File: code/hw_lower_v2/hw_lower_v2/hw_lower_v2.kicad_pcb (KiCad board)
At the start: 4 copper layers, 102 x 104.8 mm, 115 parts, among them J1 Screw_Terminal_01x01, J14 Conn_01x02, J2 Screw_Terminal_01x01, J3 Screw_Terminal_01x01, J4 Screw_Terminal_01x01, J5 Screw_Terminal_01x01, J6 Screw_Terminal_01x01, J7 Conn_01x06_Pin, J8 Conn_02x20_Odd_Even, K1 AHES4191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

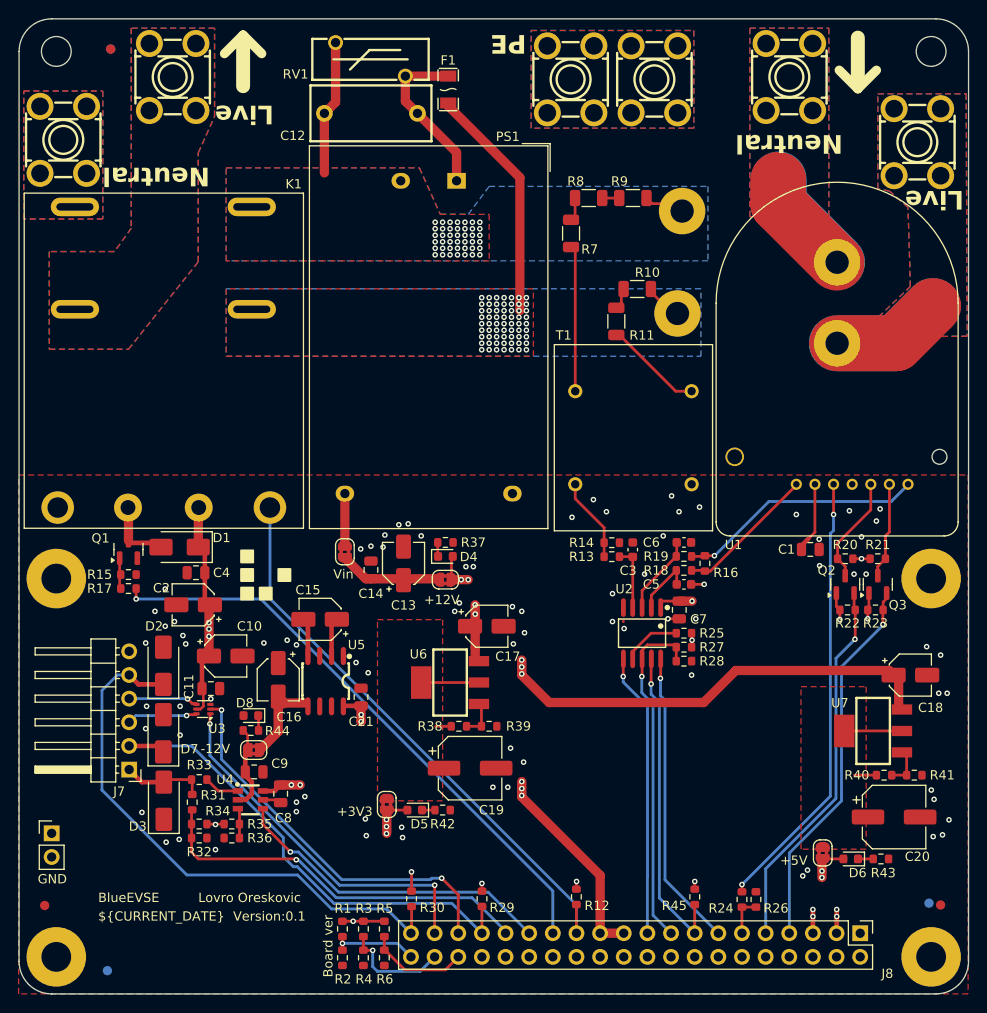
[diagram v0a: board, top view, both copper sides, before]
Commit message: made a full reposition of the whole pcb. When I get everything working, the milkv module can be on the bottom pcb and all the device specific devices can be on the other pcb. Also now conceptualy, the current board can be broken onto two, and be made into a thin long one
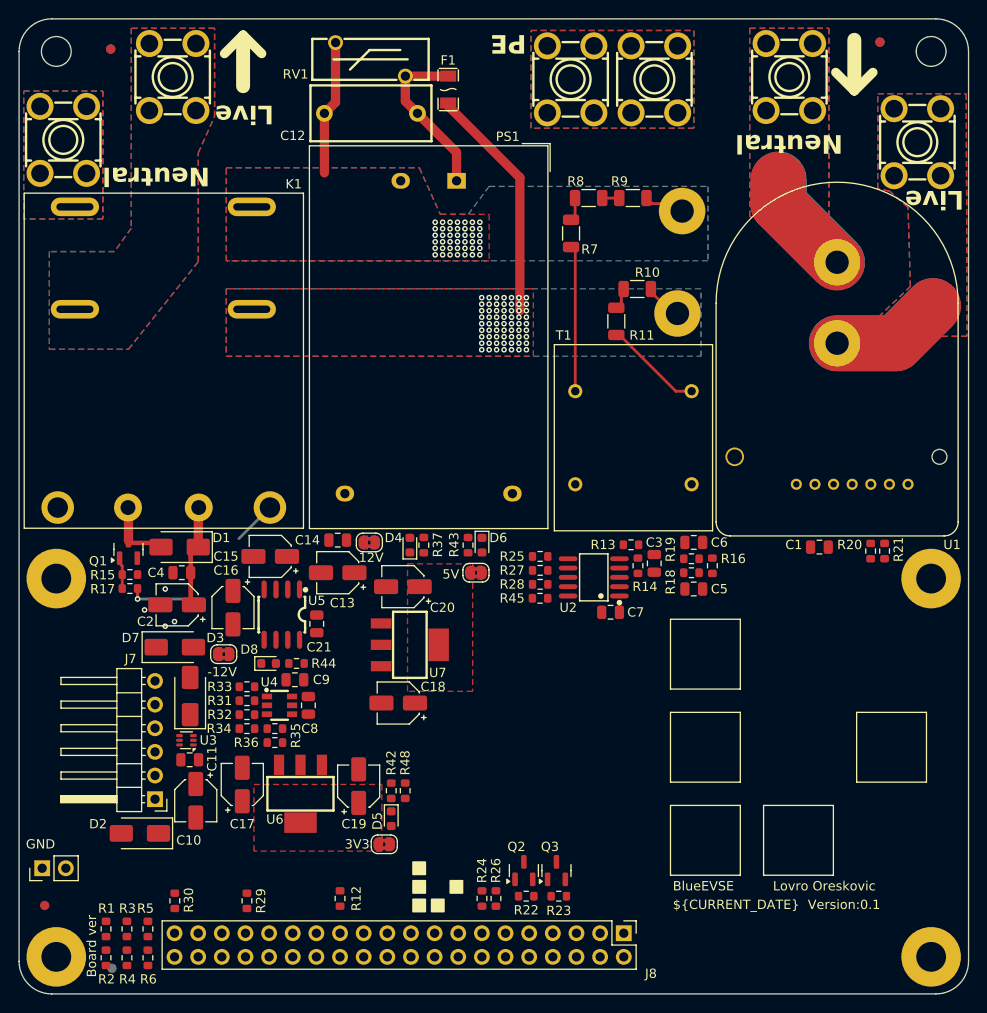
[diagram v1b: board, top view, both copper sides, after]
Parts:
- removed JP2: SolderJumper_2_Bridged, Jumper:SolderJumper-2_P1.3mm_Bridged2Bar_RoundedPad1.0x1.5mm
- removed R38: 75R, Resistor_SMD:R_0603_1608Metric
- removed R39, R41: 120R, Resistor_SMD:R_0603_1608Metric
- removed R40: 39R, Resistor_SMD:R_0603_1608Metric
- added R48: 510R, Resistor_SMD:R_0603_1608Metric, F.Cu at (141.5, 182.9)
- C19, C20: value 100u -> 10u; footprint Capacitor_SMD:CP_Elec_6.3x5.4 -> Capacitor_SMD:CP_Elec_4x5.4
- C3, C5, C6: value 33n -> 100n; footprint Capacitor_SMD:C_0603_1608Metric -> Capacitor_SMD:C_0805_2012Metric
- R15, R31: value 200K 1% -> 200K
- R17, R33: value 510R -> 820R
- R35, R36: value 10K -> 200K
- R37: value 120R -> 510R
- R42: value 75R -> 510R
- U6: value AMS1117 -> AMS1117-33
- U7: value AMS1117 -> AMS1117-5
- moved FID5 92.9 mm to (192.5, 102.5)
- moved FID3 92.7 mm to (192.5, 102.5)
- moved C20 58.3 mm to (141.2, 161.0), turned to 180 degrees
- moved R43 55.7 mm to (148.2, 156.5), turned to -90 degrees
- moved C18 55.1 mm to (140.7, 173.5), turned to 180 degrees
- moved D6 52.0 mm to (149.7, 156.5), turned to -90 degrees
- moved U7 50.6 mm to (142.0, 167.2), turned to 180 degrees
- moved JP5 47.9 mm to (149.1, 159.5), turned to 180 degrees
- moved Q2 46.2 mm to (154.2, 191.5)
- moved Q3 46.2 mm to (157.7, 191.5)
- moved R22 46.2 mm to (154.5, 194.2)
- moved R23 45.9 mm to (158.0, 194.2)
- moved R45 36.1 mm to (156.0, 162.2), turned to 0 degrees
- moved C17 31.3 mm to (124.0, 182.2), turned to 90 degrees
- moved R24 27.9 mm to (149.7, 194.5)
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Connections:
- D8 pad 1: Net-(D8-K) -> -12V
- D8 pad 2: GND -> Net-(D8-A)
- J7 pad 1: /EVSE control and status/CONTROL_PILOT_OUT -> /EVSE control and status/LOCK_SENSE
- J7 pad 2: /EVSE control and status/PROXIMITY_PILOT -> GND
- J7 pad 5: /EVSE control and status/LOCK_SENSE -> /EVSE control and status/CONTROL_PILOT_OUT
- J7 pad 6: GND -> /EVSE control and status/PROXIMITY_PILOT
- PS1 pad 4: Net-(JP2-B) -> Net-(JP1-B)
- R13 pad 2: Net-(T1-SB) -> Net-(T1-SA)
- R14 pad 1: Net-(T1-SB) -> Net-(T1-SA)
- R16 pad 1: Net-(U1-CT_S2) -> Net-(U1-CT_S1)
- R16 pad 2: Net-(U1-CT_S1) -> Net-(U1-CT_S2)
- R18 pad 1: Net-(U1-CT_S1) -> Net-(U1-CT_S2)
- R19 pad 1: Net-(U1-CT_S2) -> Net-(U1-CT_S1)
- R42 pad 1: Net-(D5-K) -> GND
- R42 pad 2: GND -> Net-(D5-K)
- R44 pad 1: Net-(D8-K) -> GND
- R44 pad 2: -12V -> Net-(D8-A)
- T1 pad 3: GND -> Net-(T1-SA)
- T1 pad 4: Net-(T1-SB) -> GND
- U6 pad 1: Net-(U6-ADJ) -> GND
- U7 pad 1: Net-(U7-ADJ) -> GND
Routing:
- net +12V: track 112.3 -> 10.3 mm, vias 17 -> 1
- net /EVSE control and status/LOCK_SENSE: track 60.9 -> 0.08 mm
- net /AC/AC_RELAY_SENSE: track 62.3 -> 4.75 mm
- net /AC/AC_RELAY_PWM: track 63.6 -> 8.31 mm
- net /EVSE control and status/PROXIMITY_PILOT: track 54.3 -> 0.01 mm
- net Net-(U1-Fault): track 47.9 -> 0.00 mm, vias 2 -> 0
- net /EVSE control and status/LOCK_B: track 42.3 -> 0.00 mm, vias 2 -> 0
- net /EVSE control and status/CONTROL_PILOT_SENSE: track 41.7 -> 0.00 mm, vias 1 -> 0
- net /AC/GFCI_TEST: track 40.7 -> 0.00 mm, vias 1 -> 0
- net /AC/GFCI_CALIBRATE: track 40.4 -> 0.00 mm, vias 1 -> 0
- net /EVSE control and status/LOCK_A: track 39.5 -> 0.00 mm, vias 2 -> 0
- net /AC/POWER_MEASUREMENT_CLK: track 37.2 -> 0.00 mm, vias 1 -> 0
- net /EVSE control and status/CONTROL_PILOT_PWM: track 35.1 -> 0.00 mm, vias 1 -> 0
- net /AC/POWER_MEASUREMENT_RX: track 34.5 -> 0.01 mm, vias 1 -> 0
- net /AC/POWER_MEASUREMENT_TX: track 32.1 -> 0.00 mm, vias 1 -> 0
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- removed copper zone on F.Cu, net GND
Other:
- board text added: "12V"
- board text added: "3V3"
- board text added: "5V"
- board text removed: "+12V"
- board text removed: "+3V3"
- board text removed: "+5V"
- board text removed: "Vin"

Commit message: Relalaid out the LV part of the board.
One or two small things left to do.
Prepared for the 2.0 version of the PCB where the duo01 module can be
put on the lower board.
Also it is possible to make a sandwitch situation, and make a long thin
product.
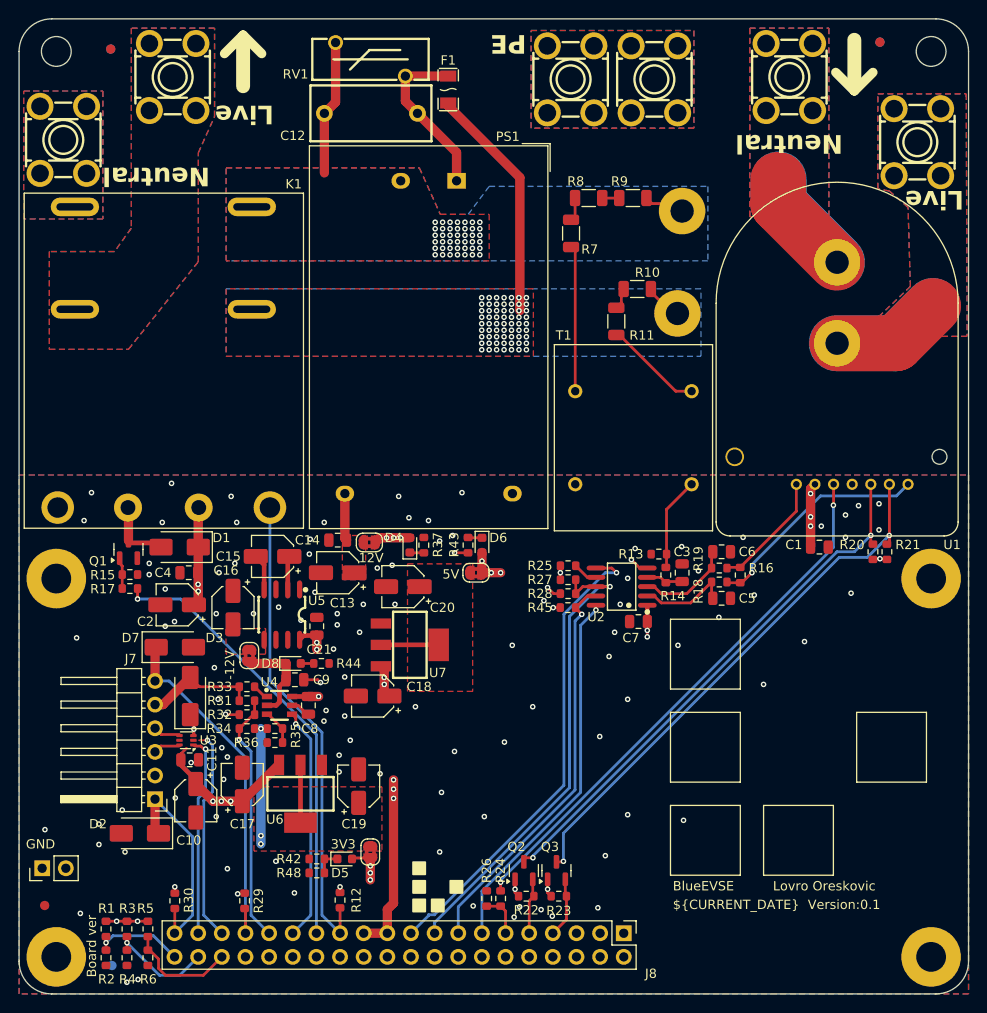
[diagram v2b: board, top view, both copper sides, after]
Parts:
- moved R48 13.0 mm to (132.0, 191.8), turned to 0 degrees
- moved R42 10.8 mm to (132.0, 190.2), turned to 0 degrees
- moved D5 6.61 mm to (135.0, 190.2), turned to 0 degrees
- moved C5 3.16 mm to (175.5, 162.2)
- moved C6 3.16 mm to (175.5, 157.2)
- moved R16 3.16 mm to (177.5, 159.8)
- moved R18 3.16 mm to (175.2, 160.5)
- moved R19 3.16 mm to (175.2, 159.0)
- moved R25 3.16 mm to (159.0, 158.8)
- moved R27 3.16 mm to (159.0, 160.2)
- moved R28 3.16 mm to (159.0, 161.8)
- moved C3 3.16 mm to (171.2, 159.5)
- moved C7 3.16 mm to (166.5, 164.8)
- moved R13 3.16 mm to (168.7, 157.5)
- moved R14 3.16 mm to (169.5, 159.8)
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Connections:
- J8 pad 3: +5V -> unconnected-(J8-Pin_3-Pad3)
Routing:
- net Net-(Q2-D): track 0.00 -> 58.7 mm, vias 0 -> 2
- net Net-(Q3-D): track 0.00 -> 58.6 mm, vias 0 -> 2
- net Net-(U1-Fault): track 0.00 -> 58.5 mm, vias 0 -> 2
- net /AC/POWER_MEASUREMENT_INFO: track 0.01 -> 51.4 mm, vias 0 -> 1
- net /AC/POWER_MEASUREMENT_CLK: track 0.00 -> 51.2 mm, vias 0 -> 1
- net +12V: track 10.3 -> 60.1 mm, vias 1 -> 16
- net /AC/AC_RELAY_SENSE: track 4.75 -> 51.6 mm
- net /AC/POWER_MEASUREMENT_RX: track 0.01 -> 43.5 mm, vias 0 -> 1
- net /AC/POWER_MEASUREMENT_TX: track 0.00 -> 40.3 mm, vias 0 -> 1
- net /AC/AC_RELAY_PWM: track 8.31 -> 48.1 mm
- net /EVSE control and status/PROXIMITY_PILOT: track 0.01 -> 38.4 mm
- net +3.3V: track 0.08 -> 34.3 mm, vias 0 -> 17
- net /EVSE control and status/CONTROL_PILOT_SENSE: track 0.00 -> 27.1 mm, vias 0 -> 1
- net /EVSE control and status/CONTROL_PILOT_PWM: track 0.00 -> 25.2 mm, vias 0 -> 1
- net Net-(U1-CT_S2): track 0.00 -> 24.4 mm, vias 0 -> 1
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- added copper zone on B.Cu, net GND
- added copper zone on F.Cu, net GND
- added copper zone on F.Cu, net Net-(JP1-B)
- added copper zone on F.Cu, net Net-(JP3-B)

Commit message: almost ready :-)
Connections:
- J8 pad 1: unconnected-(J8-Pin_1-Pad1) -> +3.3V
- J8 pad 3: unconnected-(J8-Pin_3-Pad3) -> +3.3V
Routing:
- net +12V: track 60.1 -> 61.3 mm
- net /EVSE control and status/LOCK_B: track 23.0 -> 23.7 mm
- net GND: vias 109 -> 128

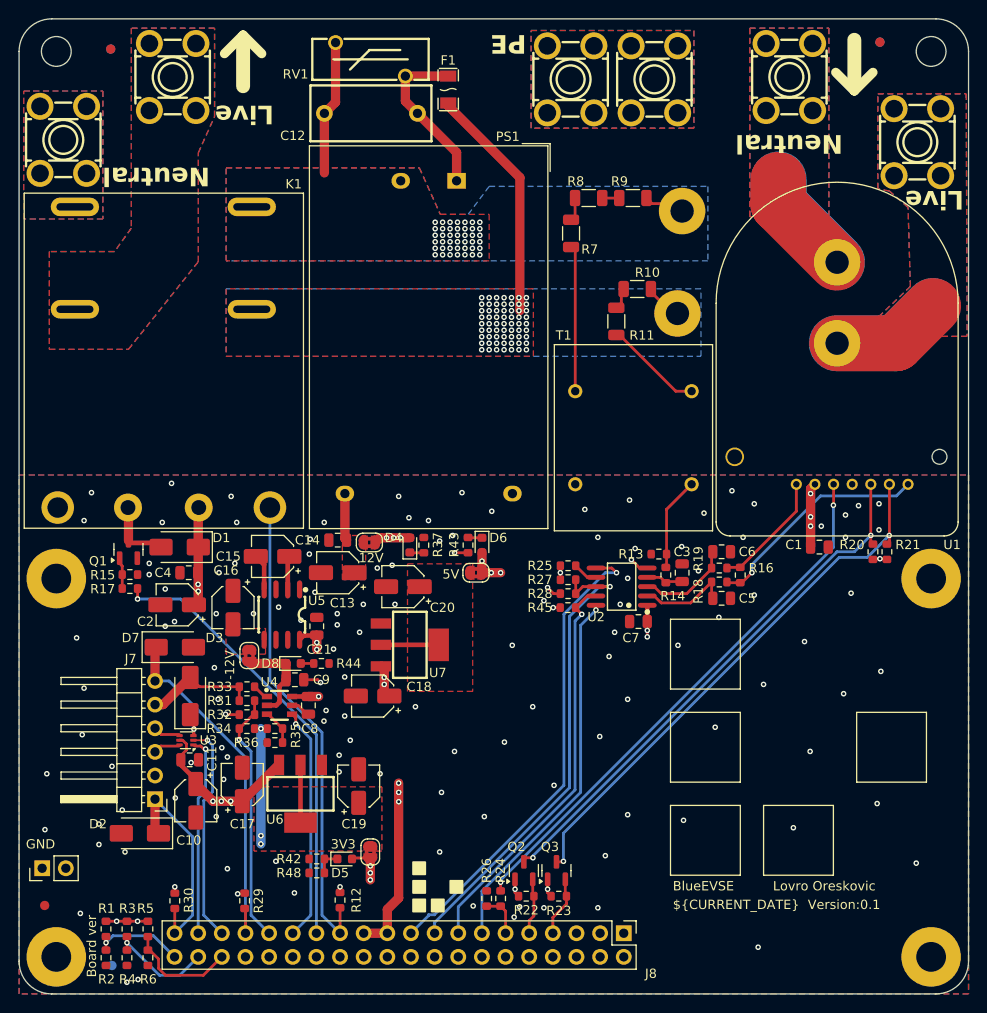
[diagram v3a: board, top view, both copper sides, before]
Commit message: add JLCPCB tooling holes and simplify further
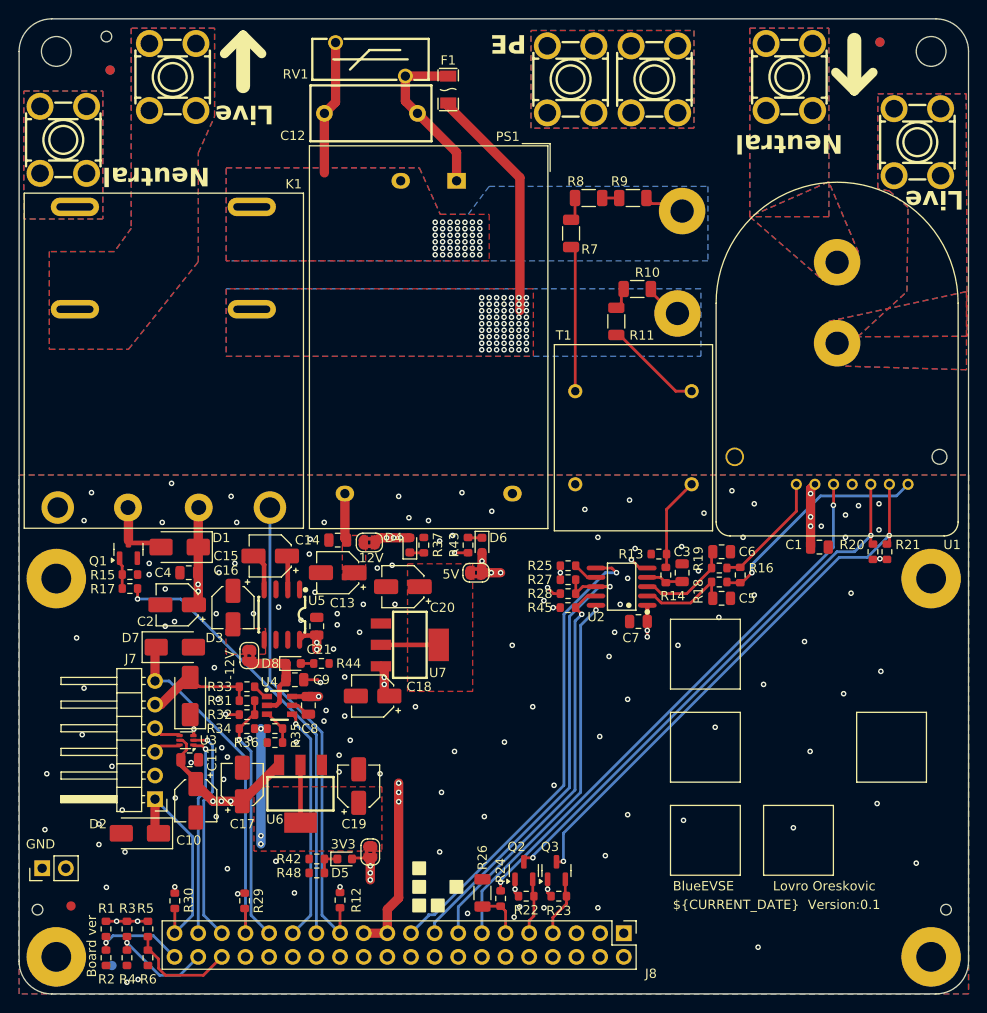
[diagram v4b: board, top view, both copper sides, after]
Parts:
- added REF**: jlcpcb_tooling_hole, multi_new:jlcpcb_tooling_hole, F.Cu at (109.4, 101.9)
- added REF**: jlcpcb_tooling_hole, multi_new:jlcpcb_tooling_hole, F.Cu at (102.0, 195.7)
- added REF**: jlcpcb_tooling_hole, multi_new:jlcpcb_tooling_hole, F.Cu at (199.6, 195.7)
- R17, R33: value 820R -> 510R
- R26: footprint Resistor_SMD:R_0603_1608Metric -> Resistor_SMD:R_1206_3216Metric
- moved FID6 2.83 mm to (105.6, 195.3)
- moved FID2 2.25 mm to (109.8, 105.5)
- moved FID4 2.25 mm to (109.8, 105.5)
- moved R26 0.75 mm to (149.8, 193.9)
- moved C15 0.25 mm to (127.0, 157.7)
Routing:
- net /AC/L_in: track 24.0 -> 0.00 mm
- net /AC/N_in: track 23.0 -> 0.00 mm
- net /AC/N_internal_power: track 19.2 -> 16.4 mm
- net GND: track 13.0 -> 11.5 mm, vias 128 -> 130
- net +12V: track 61.3 -> 59.9 mm
- net Net-(T1-AA): track 11.3 -> 10.2 mm
- net Net-(U2-IN): track 10.2 -> 9.20 mm
- net Net-(U2-IP): track 9.96 -> 9.03 mm
- net /AC/L_internal_power: track 29.6 -> 28.8 mm
- net Net-(Q2-D): track 58.7 -> 57.9 mm
- net Net-(Q1-G): track 3.15 -> 2.41 mm
- net Net-(D1-A): track 7.37 -> 6.66 mm
- net /EVSE control and status/LOCK_SENSE: track 23.5 -> 22.8 mm
- net Net-(JP3-B): track 0.61 -> 0.00 mm
- net /EVSE control and status/CONTROL_PILOT_OUT: track 12.5 -> 11.9 mm
- added copper zone on In2.Cu, net /AC/N_in
